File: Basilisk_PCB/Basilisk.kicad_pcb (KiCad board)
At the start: 2 copper layers, 57 parts, among them J1 Conn_01x04, J2 HUB75E, J3 Barrel_Jack, J4 USB_C_Receptacle_USB2.0, Q1 S8050, Q2 S8050, SW1 IO0, SW2 RST, U1 AT25SF081-SSHD-X, U2 ESP32-WROOM-32D, U3 MLX90640, U4 TXS0108EPW, U5 TXS0108EPW, U6 TPS54560BDDA, U7 AMS1117-3.3, U8 FT231XS

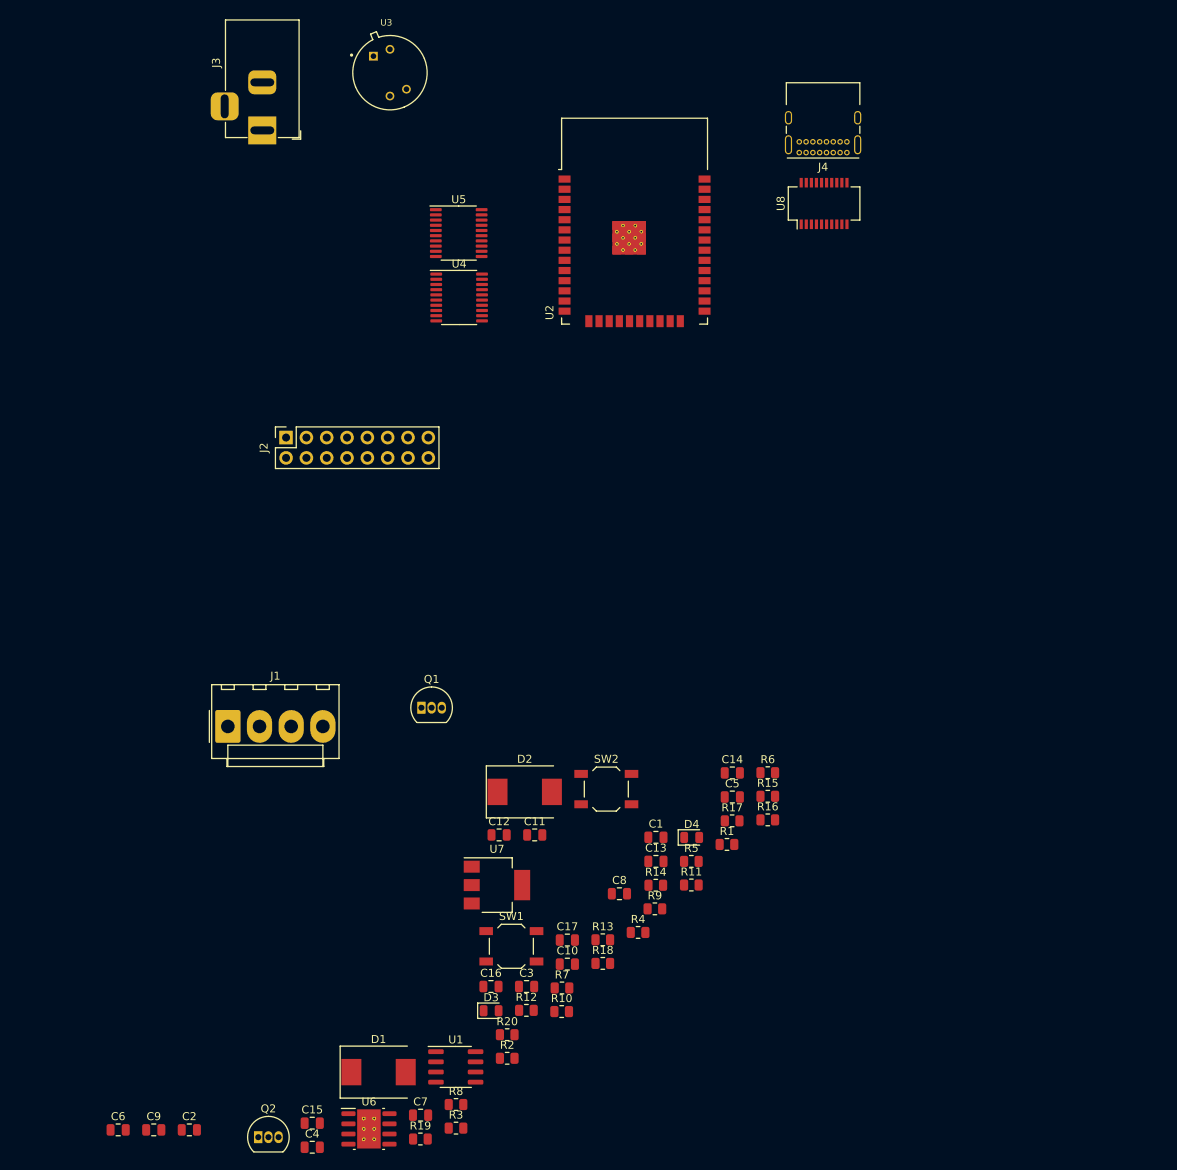
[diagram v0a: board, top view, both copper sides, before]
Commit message: add CAD model of matrix
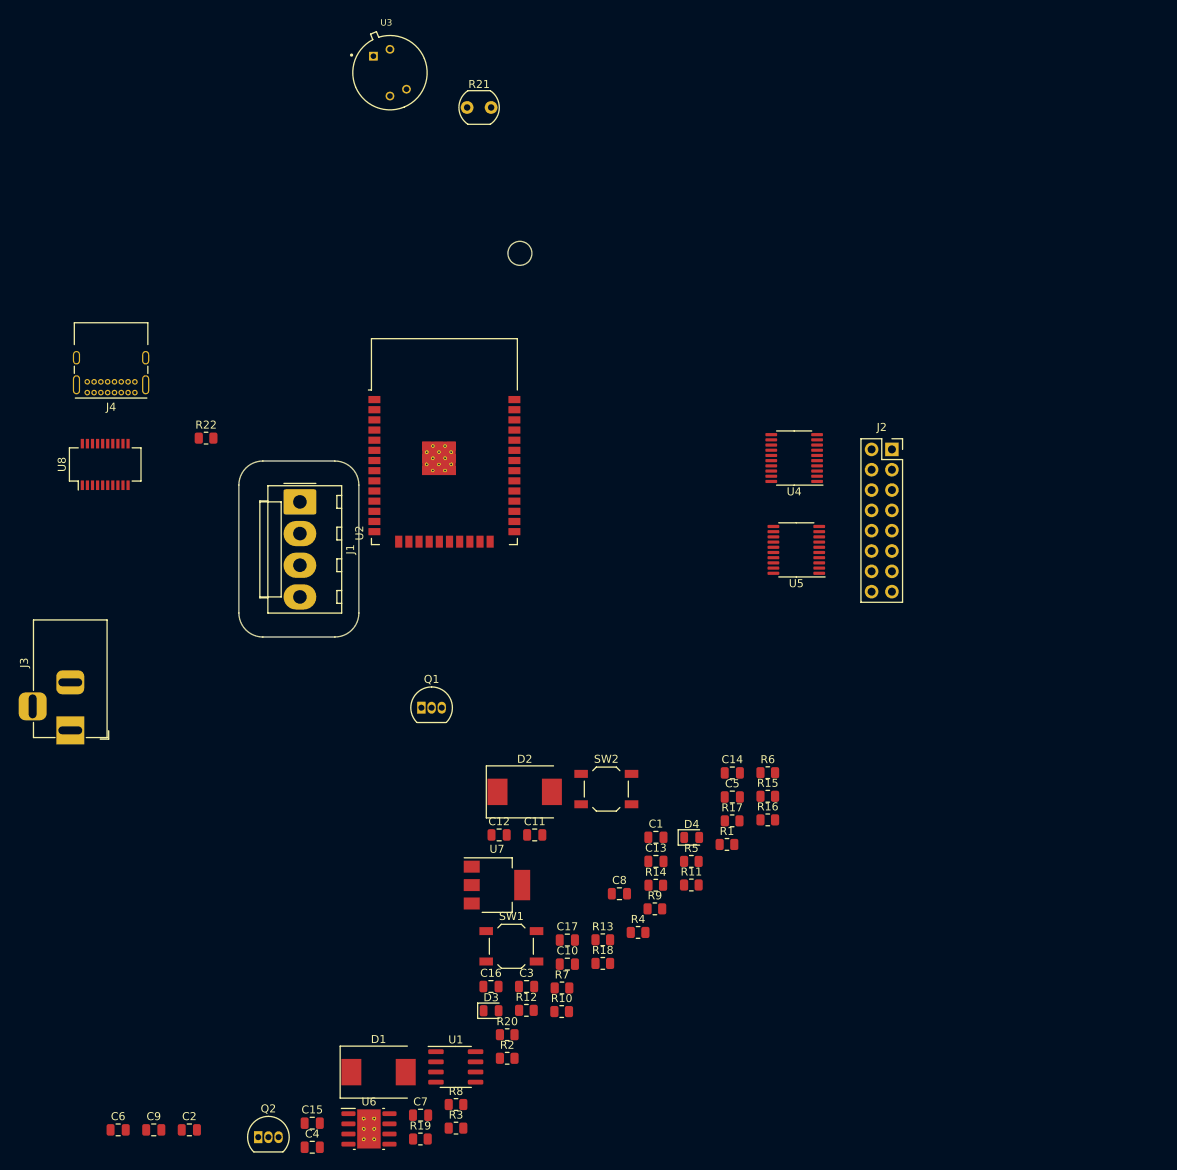
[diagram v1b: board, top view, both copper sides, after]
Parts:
- added R21: PDV-P8103, OptoDevice:R_LDR_5.0x4.1mm_P3mm_Vertical, F.Cu at (136.4, 19.8)
- added R22: 53.6k, Resistor_SMD:R_0805_2012Metric, F.Cu at (103.8, 61.1)
- moved U8 95.6 mm to (91.2, 64.4)
- moved J4 93.9 mm to (94.9, 55.4)
- moved J3 78.7 mm to (86.8, 97.6)
- moved J2 75.7 mm to (189.5, 62.5), turned to 0 degrees
- moved U5 57.9 mm to (177.6, 75.1), turned to 180 degrees
- moved U4 46.4 mm to (177.3, 63.6), turned to 180 degrees
- moved U2 36.4 mm to (133.6, 64.5)
- moved J1 29.5 mm to (115.5, 69.1), turned to -90 degrees
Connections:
- U2 pad 6: unconnected-(U2-Pad6) -> Net-(U2-Pad6)
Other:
- board outline added: 36.6 x 49.5 mm
- board text added: "For Instructional Use Only."
- board text added: "SOLIDWORKS Educational Product."

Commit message: set up fixed components on board
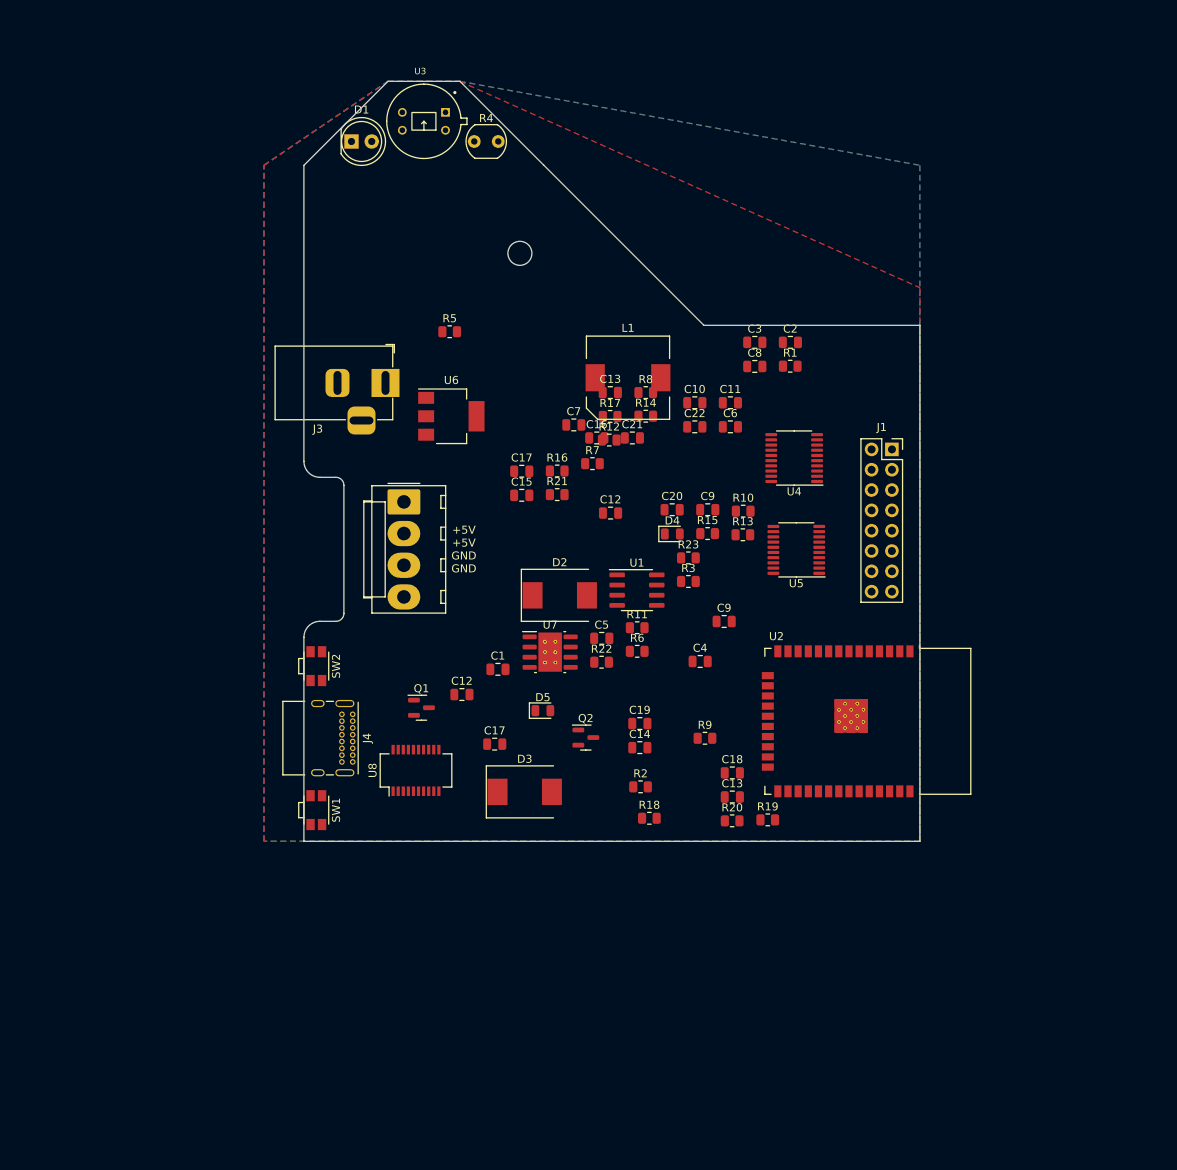
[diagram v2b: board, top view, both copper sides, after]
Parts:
- added C10: 0.1uf, Capacitor_SMD:C_0805_2012Metric, F.Cu at (164.9, 56.7)
- added C11: 0.1uf, Capacitor_SMD:C_0805_2012Metric, F.Cu at (169.3, 56.7)
- added C16: 0.1uf, Capacitor_SMD:C_0805_2012Metric, F.Cu at (152.6, 61.1)
- added C2: 0.1uf, Capacitor_SMD:C_0805_2012Metric, F.Cu at (176.8, 49.1)
- added C21: 0.1uf, Capacitor_SMD:C_0805_2012Metric, F.Cu at (157.1, 61.1)
- added C22: 0.1uf, Capacitor_SMD:C_0805_2012Metric, F.Cu at (164.9, 59.7)
- added C3: 0.1uf, Capacitor_SMD:C_0805_2012Metric, F.Cu at (172.4, 49.1)
- added C6: 0.1uf, Capacitor_SMD:C_0805_2012Metric, F.Cu at (169.3, 59.7)
- added C8: 0.1uf, Capacitor_SMD:C_0805_2012Metric, F.Cu at (172.4, 52.1)
- added D1: STATUS, LED_THT:LED_D5.0mm_Clear, F.Cu at (121.9, 24.0)
- added L1: 7.2uH, Inductor_SMD:L_Wuerth_WE-PDF, F.Cu at (156.5, 53.5)
- added R1: 68, Resistor_SMD:R_0805_2012Metric, F.Cu at (176.8, 52.1)
- Q1, Q2: footprint Package_TO_SOT_THT:TO-92_Inline -> Package_TO_SOT_SMD:SOT-23
- SW1, SW2: footprint Button_Switch_SMD:SW_SPST_TL3342 -> Button_Switch_SMD:SW_SPST_EVQP7A
- moved C12 98.7 mm to (154.3, 70.5)
- moved C9 95.5 mm to (168.5, 84.0)
- moved C4 86.6 mm to (165.5, 89.0)
- moved C14 64.6 mm to (158.0, 99.8)
- moved C19 64.6 mm to (158.0, 96.8)
- moved Q2 64.6 mm to (151.2, 98.5)
- moved C20 63.8 mm to (162.0, 70.0)
- moved D4 63.8 mm to (162.1, 73.1)
- moved R10 63.8 mm to (170.9, 70.2)
- moved R11 63.8 mm to (157.7, 84.8)
- moved R22 63.8 mm to (153.2, 89.1)
- moved R3 63.8 mm to (164.1, 79.0)
- moved C9 63.8 mm to (166.5, 70.0)
- moved R13 63.8 mm to (170.9, 73.2)
- moved R15 63.8 mm to (166.5, 73.0)
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- renumbered C6 to C12, C5 to C13, C4 to C14, C10 to C15, C11 to C17, C14 to C18, C15 to C19, C16 to C20, C2 to C4, C7 to C5, C8 to C7, C3 to C9, D1 to D2, D2 to D3, D3 to D4, D4 to D5, J2 to J1, J1 to J2, R7 to R10, R8 to R11, R9 to R12, R10 to R13, R11 to R14, R12 to R15, R13 to R16, R14 to R17, R15 to R18, R16 to R19, R1 to R2, R17 to R20, R18 to R21, R19 to R22, R20 to R23, R2 to R3, R21 to R4, R22 to R5, R3 to R6, R4 to R7, R5 to R8, R6 to R9, U7 to U6, U6 to U7
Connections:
- C12 pad 1: +12V -> GND
- C12 pad 2: GND -> +12V
- C13 pad 1: +12V -> GND
- C13 pad 2: GND -> +12V
- C14 pad 1: +12V -> GND
- C14 pad 2: GND -> +12V
- Q2 pad 3: /IO0 -> /CMD
- R12 pad 1: /IO0 -> /CMD
- R19 pad 2: /IO0 -> /CMD
- SW1 pad 2: unconnected-(SW1-Pad2) -> GND
- SW2 pad 2: unconnected-(SW2-Pad2) -> GND
- U1 pad 2: /DO -> /MISO
- U1 pad 5: /DI -> /MOSI
- U2 pad 25: /IO0 -> /CMD
- U2 pad 29: /CMD -> /OE.3
- U5 pad 12: /IO0 -> /OE.3
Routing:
- added copper zone on B.Cu, net +3.3V
- added copper zone on F.Cu, net GND
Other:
- board size 36.6 x 49.5 mm -> 77 x 95 mm
- board text added: "+5V +5V GND GND"

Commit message: Routed PCB
Routed most of PCB
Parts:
- C12, C13: value C_Small -> 0.1uf
- C17: value 100n -> 47pf
- moved C17 87.6 mm to (216.1, 56.3)
- moved C12 76.6 mm to (176.9, 28.6)
- moved C12 75.5 mm to (220.6, 34.2)
- moved C18 74.8 mm to (218.2, 46.1)
- moved C4 74.2 mm to (221.7, 40.5)
- moved C13 73.8 mm to (220.8, 52.9)
- moved C14 70.8 mm to (156.8, 29.0)
- moved C7 69.5 mm to (212.4, 29.5)
- moved C1 68.9 mm to (171.6, 28.6)
- moved C19 68.1 mm to (160.7, 28.7)
- moved C5 64.7 mm to (198.2, 39.6)
- moved C9 63.5 mm to (206.0, 32.8)
- moved C15 57.0 mm to (192.9, 40.4)
- moved C17 55.5 mm to (185.8, 29.6)
- moved R8 54.2 mm to (124.5, 97.4)
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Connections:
- C12 pad 1: VBUS -> GND
- C12 pad 2: GND -> +12V
- C13 pad 1: +3.3V -> GND
- C13 pad 2: GND -> +12V
- C17 pad 1: /3.3V_FTDI -> Net-(C17-Pad1)
- C9 pad 1: +5V -> +3.3V
- J1 pad 5: /R2.2 -> /R2.5
- U2 pad 23: /B.3 -> /OE.3
- U2 pad 29: /OE.3 -> /B.3
- U4 pad 1: /G1.5 -> unconnected-(U4-Pad1)
- U4 pad 12: unconnected-(U4-Pad12) -> /R1.3
- U4 pad 13: unconnected-(U4-Pad13) -> /G1.3
- U4 pad 14: /LAT.3 -> /B1.3
- U4 pad 15: /D.3 -> /R2.3
- U4 pad 16: /B.3 -> /G2.3
- U4 pad 17: /E.3 -> /B2.3
- U4 pad 18: /G2.3 -> unconnected-(U4-Pad18)
- U4 pad 20: /G1.3 -> unconnected-(U4-Pad20)
- U4 pad 3: /G2.5 -> unconnected-(U4-Pad3)
- U4 pad 4: /E.5 -> /B2.5
- U4 pad 5: /B.5 -> /G2.5
- U4 pad 6: /D.5 -> /R2.5
- U4 pad 7: /LAT.5 -> /B1.5
- U4 pad 8: unconnected-(U4-Pad8) -> /G1.5
- U4 pad 9: unconnected-(U4-Pad9) -> /R1.5
- U5 pad 1: /R1.5 -> /OE.5
- U5 pad 12: /OE.3 -> /E.3
- U5 pad 13: /CLK.3 -> /B.3
- U5 pad 14: /C.3 -> /A.3
- U5 pad 15: /A.3 -> /D.3
- U5 pad 16: /B2.3 -> /C.3
- U5 pad 17: /R2.3 -> /LAT.3
- U5 pad 18: /B1.3 -> /CLK.3
- U5 pad 20: /R1.3 -> /OE.3
- U5 pad 3: /B1.5 -> /CLK.5
- U5 pad 4: /R2.2 -> /LAT.5
- U5 pad 5: /B2.5 -> /C.5
- U5 pad 6: /A.5 -> /D.5
- U5 pad 7: /C.5 -> /A.5
- U5 pad 8: /CLK.5 -> /B.5
- U5 pad 9: /OE.5 -> /E.5
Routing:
- net +3.3V: track 0.00 -> 149.6 mm, vias 0 -> 16
- net /SCL: track 0.00 -> 132.5 mm, vias 0 -> 2
- net /SDA: track 0.00 -> 118.3 mm, vias 0 -> 6
- net +5V: track 0.00 -> 92.3 mm, vias 0 -> 10
- net VBUS: track 0.00 -> 92.0 mm, vias 0 -> 8
- net Net-(D1-Pad1): track 0.00 -> 86.8 mm, vias 0 -> 2
- net Net-(R4-Pad2): track 0.00 -> 84.0 mm, vias 0 -> 2
- net /CMD: track 0.00 -> 82.6 mm, vias 0 -> 6
- net /USB>ESP: track 0.00 -> 78.8 mm, vias 0 -> 2
- net /EN: track 0.00 -> 75.2 mm, vias 0 -> 4
- net /ESP>USB: track 0.00 -> 66.5 mm, vias 0 -> 4
- net /B.3: track 0.00 -> 58.5 mm
- net /D.3: track 0.00 -> 54.5 mm
- net /R1.3: track 0.00 -> 44.3 mm
- net /LAT.3: track 0.00 -> 42.7 mm
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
